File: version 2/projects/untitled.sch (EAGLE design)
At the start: 27 parts, among them IC1 LM1117IMPX-3.3, U1 FT232RLSSOP, U2 MCP73831, X2 USB-SMD-NS

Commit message: connected \!DTR Pin to RST
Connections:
- removed net N$7: U$1.RST1
- net DTR: now also U$1.RST1
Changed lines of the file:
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@@
-</segment>
-</net>
-<net name="N$7" class="0">
-<segment>
-<pinref part="U$1" gate="G$1" pin="RST1"/>
-<wire x1="154.94" y1="408.94" x2="144.78" y2="408.94" width="0.1524" layer="91"/>
-<label x="144.78" y="408.94" size="1.778" layer="95" rot="R180" xref="yes"/>
 </segment>
 </net>
@@
 <pinref part="U1" gate="G$1" pin="DTR"/>
 </segment>
+<segment>
+<pinref part="U$1" gate="G$1" pin="RST1"/>
+<wire x1="154.94" y1="408.94" x2="144.78" y2="408.94" width="0.1524" layer="91"/>
+<label x="144.78" y="408.94" size="1.778" layer="95" rot="R180" xref="yes"/>
+</segment>
 </net>

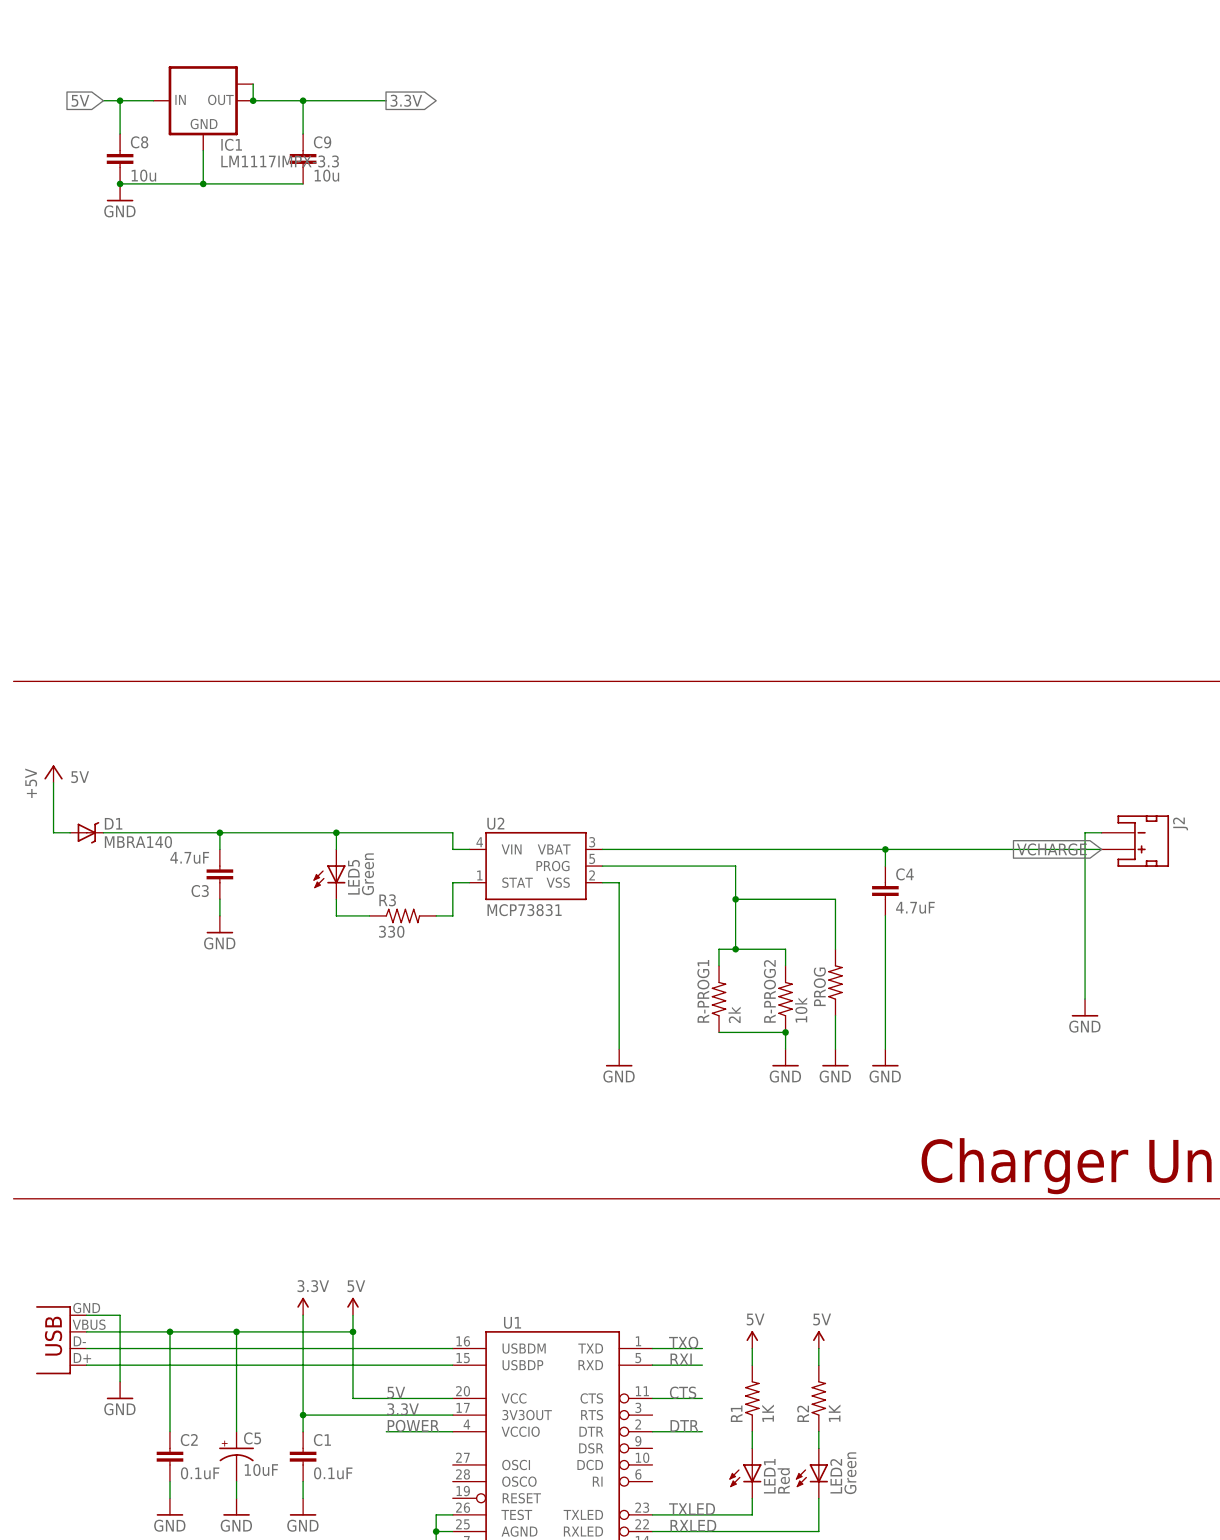
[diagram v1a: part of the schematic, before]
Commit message: reworked layout. Added voltage controller and discharging mechanism
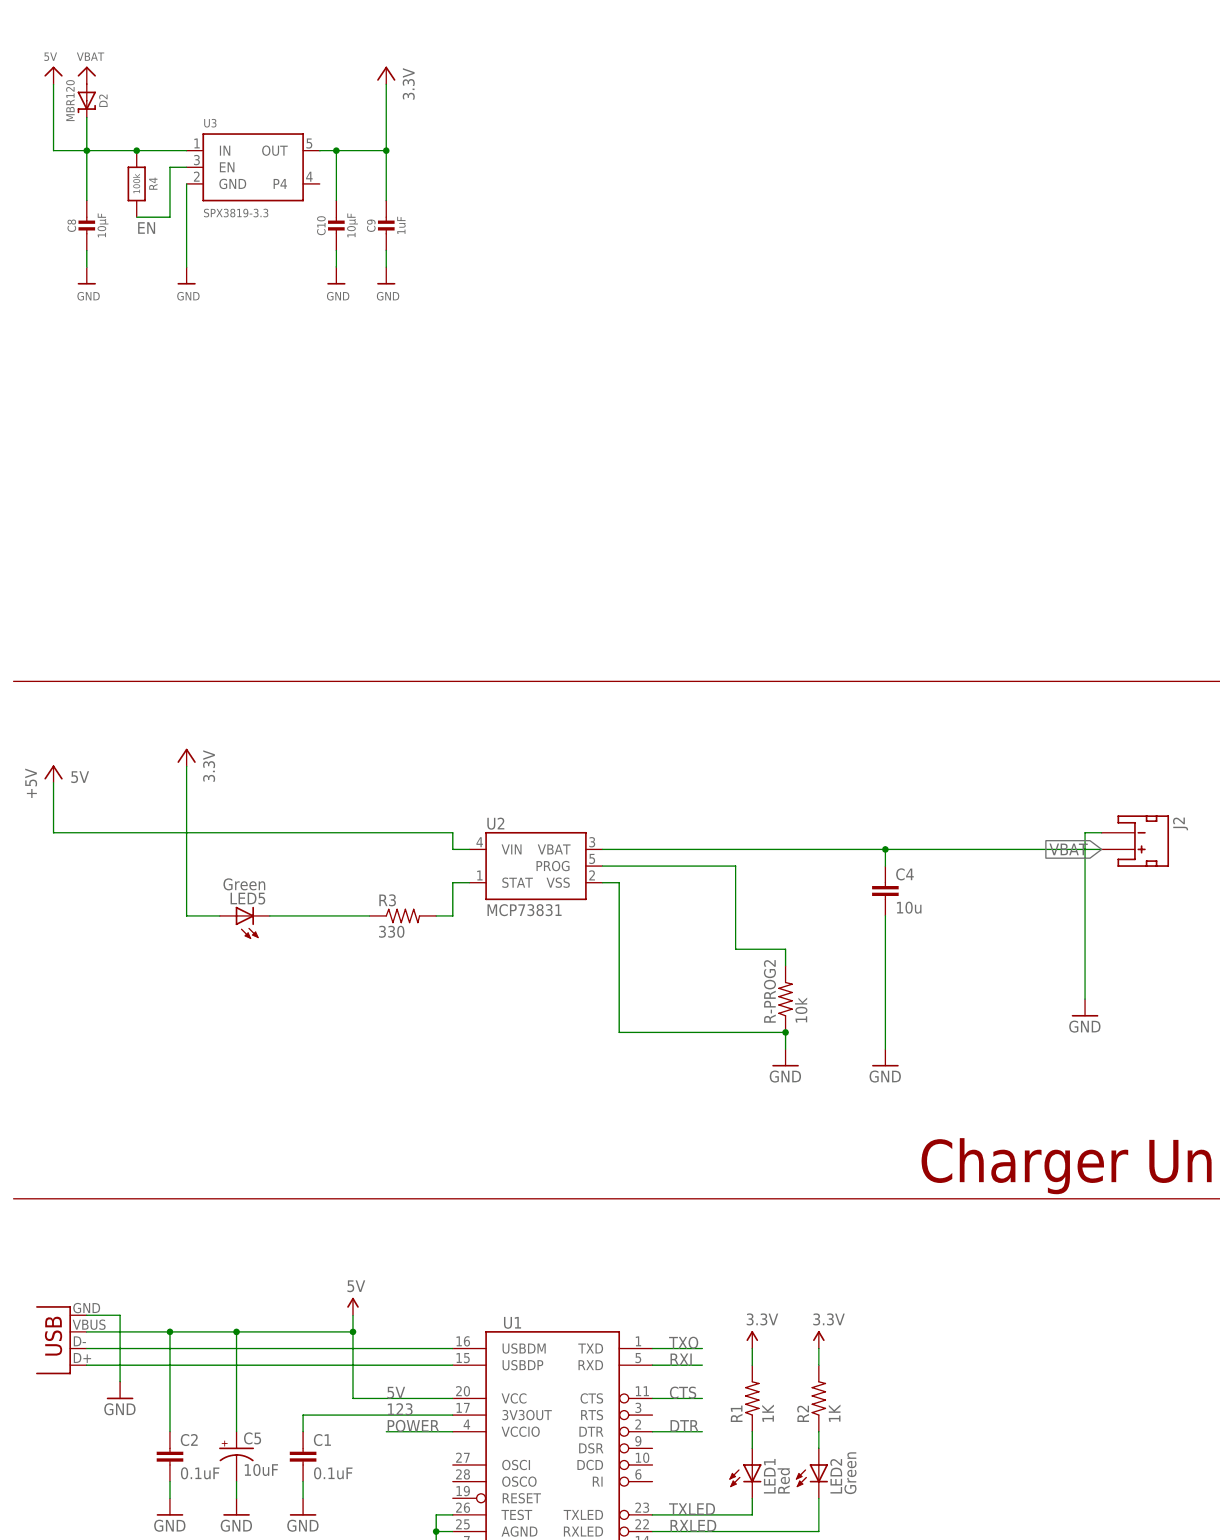
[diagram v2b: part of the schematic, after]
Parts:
- removed C3: 4.7uF, SparkFun-Capacitors:4.7UF-6.3V-10%(0603)0603
- removed D1: MBRA140, SparkFun-DiscreteSemi:MBRA140
- removed IC1: LM1117IMPX-3.3, lm1117:LM1117IMPX-3.3
- removed PROG: (no value), SparkFun-Resistors:RESISTORAXIAL-0.3
- removed R-PROG1: 2k, SparkFun-Resistors:2.0KOHM1/10W5%(0603)
- added C10: 10µF, microbuilder:CAP_CERAMIC0805-NOOUTLINE
- added D2: MBR120, microbuilder:DIODE-SCHOTTKYSOD-123
- added R4: 100k, microbuilder:RESISTOR_0603_NOOUT
- added U3: SPX3819-3.3, microbuilder:VREG_SOT23-5
- C4: value 4.7uF -> 10u
- C8: value 10u -> 10µF; device rcl:C-EUC0805 -> microbuilder:CAP_CERAMIC0805-NOOUTLINE
- C9: value 10u -> 1uF; device rcl:C-EUC0805 -> microbuilder:CAP_CERAMIC0603_NO
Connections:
- removed net N$3: C3.2, D1.C, LED5.A, U2.VIN
- removed net VCHARGE: C4.1, J2.+, U2.VBAT
- new net +3V3: LED5.A
- new net 123: C1.1, U1.3V3OUT
- new net EN: R4.2, U3.EN
- new net VBAT: C4.1, D2.A, J2.+, U2.VBAT
- net 3.3V: now also C10.1, R1.2, R2.2, U3.OUT; no longer C1.1, IC1.OUT, IC1.OUT1, U1.3V3OUT
- net 5V: now also D2.C, R4.1, U2.VIN, U3.IN; no longer D1.A, IC1.IN, R1.2, R2.2
- net GND: now also C10.2, U3.GND; no longer C3.1, IC1.GND, PROG.1, R-PROG1.1
- net LOL: no longer PROG.2, R-PROG1.2
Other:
- moved on the sheet: C8, C9, LED5

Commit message: initial commit
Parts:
- renumbered J$1 to J$2
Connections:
- net GND: now also J$2.GND@1, J$2.GND@2
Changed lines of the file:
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@@
 <part name="GND13" library="supply1" deviceset="GND" device=""/>
 <part name="GND16" library="supply1" deviceset="GND" device=""/>
-<part name="J$1" library="_c2h" deviceset="ANTENNA" device="TINY"/>
 <part name="C8" library="microbuilder" deviceset="CAP_CERAMIC" device="0805-NOOUTLINE" value="10µF"/>
 <part name="C9" library="microbuilder" deviceset="CAP_CERAMIC" device="0603_NO" value="1uF"/>
@@
 <part name="R4" library="microbuilder" deviceset="RESISTOR" device="_0603_NOOUT" value="100k"/>
 <part name="+3V1" library="supply1" deviceset="+3V3" device="" value="3.3V"/>
+<part name="J$2" library="_c2h" deviceset="ANTENNA" device="TINY"/>
 </parts>
 <sheets>
@@
 <instance part="GND13" gate="1" x="93.98" y="383.54"/>
 <instance part="GND16" gate="1" x="114.3" y="398.78"/>
-<instance part="J$1" gate="1" x="121.92" y="426.72"/>
 <instance part="C8" gate="G$1" x="-154.94" y="403.86"/>
 <instance part="C9" gate="G$1" x="-109.22" y="403.86"/>
@@
 <instance part="R4" gate="G$1" x="-147.32" y="411.48" rot="R270"/>
 <instance part="+3V1" gate="G$1" x="-139.7" y="325.12" rot="MR0"/>
+<instance part="J$2" gate="1" x="121.92" y="426.72"/>
 </instances>
 <busses>
@@
 <wire x1="114.3" y1="408.94" x2="114.3" y2="401.32" width="0.1524" layer="91"/>
 <pinref part="GND16" gate="1" pin="GND"/>
-<pinref part="J$1" gate="1" pin="GND@0"/>
-<pinref part="J$1" gate="1" pin="GND@3"/>
-<wire x1="119.38" y1="421.64" x2="119.38" y2="414.02" width="0.1524" layer="91"/>
+<wire x1="119.38" y1="421.64" x2="119.38" y2="419.1" width="0.1524" layer="91"/>
+<wire x1="119.38" y1="419.1" x2="119.38" y2="416.56" width="0.1524" layer="91"/>
+<wire x1="119.38" y1="416.56" x2="119.38" y2="414.02" width="0.1524" layer="91"/>
 <wire x1="114.3" y1="408.94" x2="119.38" y2="414.02" width="0.1524" layer="91"/>
+<pinref part="J$2" gate="1" pin="GND@0"/>
+<pinref part="J$2" gate="1" pin="GND@1"/>
+<junction x="119.38" y="419.1"/>
+<pinref part="J$2" gate="1" pin="GND@2"/>
+<junction x="119.38" y="416.56"/>
+<pinref part="J$2" gate="1" pin="GND@3"/>
 <junction x="119.38" y="414.02"/>
 </segment>
@@
 <wire x1="106.68" y1="401.32" x2="106.68" y2="403.86" width="0.1524" layer="91"/>
 <wire x1="106.68" y1="403.86" x2="116.84" y2="414.02" width="0.1524" layer="91"/>
-<pinref part="J$1" gate="1" pin="SIGNAL"/>
 <wire x1="116.84" y1="426.72" x2="116.84" y2="414.02" width="0.1524" layer="91"/>
-</segment>
-</net>
+<pinref part="J$2" gate="1" pin="SIGNAL"/>
+</segment>
+</net>
